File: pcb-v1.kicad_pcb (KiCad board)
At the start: 2 copper layers, 177 x 161.5 mm, 32 parts, among them J1 Conn_01x03_Socket, J10 Screw_Terminal_01x04, J11 Screw_Terminal_01x04, J12 Screw_Terminal_01x04, J13 Screw_Terminal_01x04, J14 Screw_Terminal_01x06, J15 Conn_01x06_Pin, J2 Conn_01x03_Socket, J3 Conn_01x03_Socket, J4 Conn_01x03_Socket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

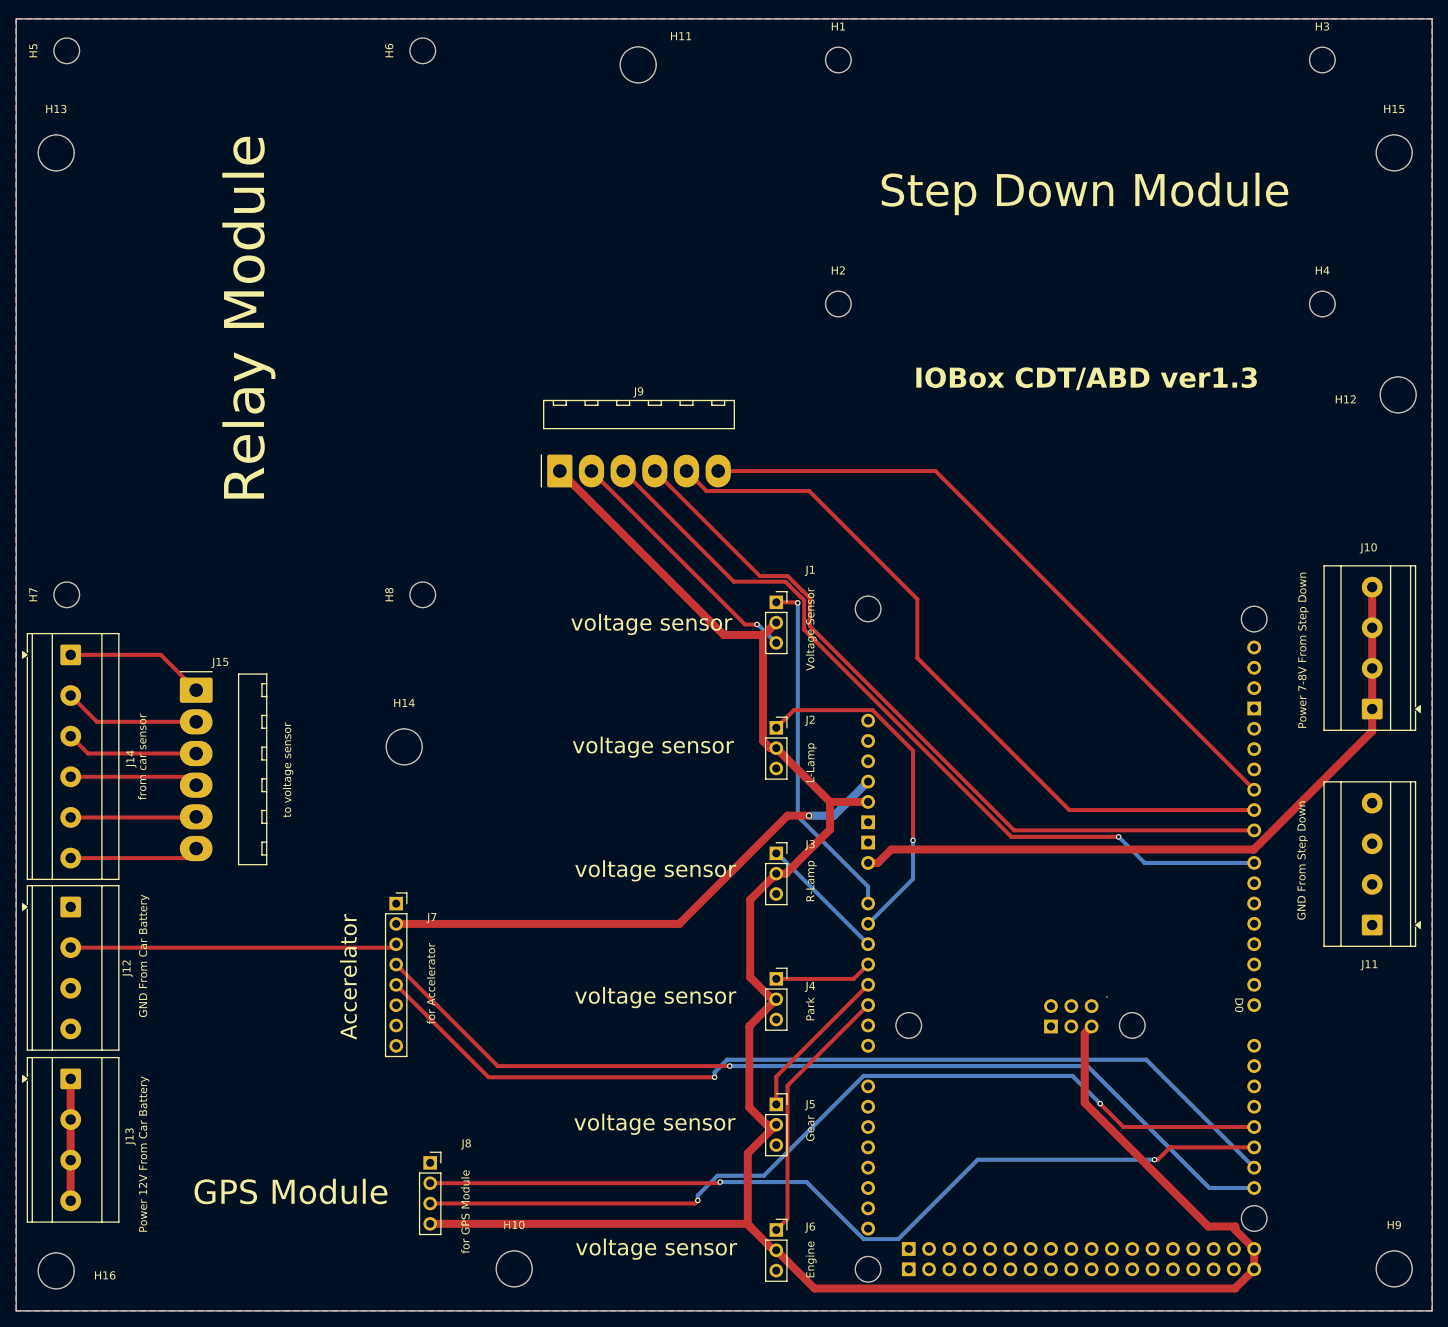
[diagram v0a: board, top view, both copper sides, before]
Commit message: adjust foot print to small size
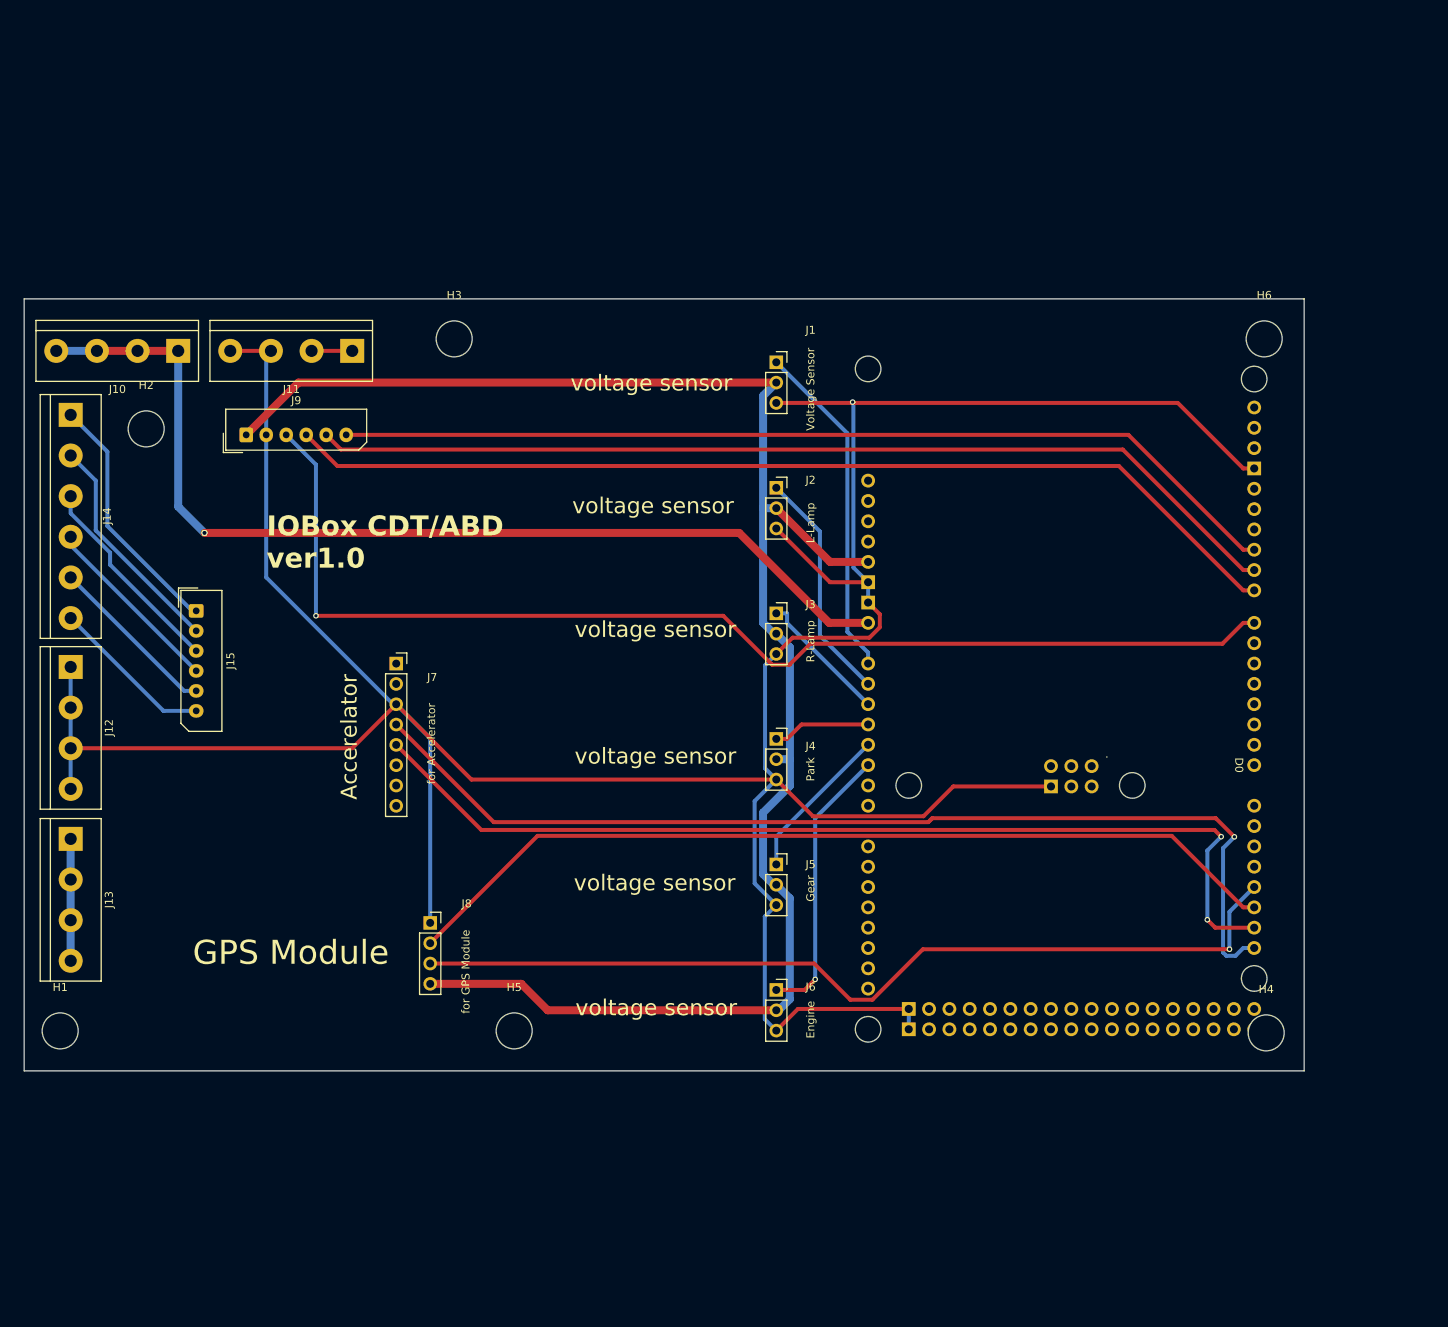
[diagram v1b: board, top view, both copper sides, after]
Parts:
- removed H10, H11, H12, H13, H14, H15, H16, H9: MountingHole, MountingHole:MountingHole_4.5mm
- removed H7, H8: MountingHole, MountingHole:MountingHole_3.2mm_M3
- H1, H2, H3, H4, H5, H6: footprint MountingHole:MountingHole_3.2mm_M3 -> MountingHole:MountingHole_4.5mm
- J10, J11, J12, J13: footprint TerminalBlock_Phoenix:TerminalBlock_Phoenix_MKDS-3-4-5.08_1x04_P5.08mm_Horizontal -> TerminalBlock-bornier:TerminalBlock_bornier-4_P5.08mm
- J14: footprint TerminalBlock_Phoenix:TerminalBlock_Phoenix_MKDS-3-6-5.08_1x06_P5.08mm_Horizontal -> TerminalBlock-bornier:TerminalBlock_bornier-6_P5.08mm
- J15, J9: footprint Connector_Molex:Molex_KK-396_A-41792-0006_1x06_P3.96mm_Horizontal -> Connector_Molex:Molex_SPOX_5267-06A_1x06_P2.50mm_Vertical
- moved J10 155.8 mm to (82.8, 58.0), turned to 180 degrees
- moved H1 155.5 mm to (68.0, 143.0)
- moved J11 146.3 mm to (104.5, 58.0), turned to 180 degrees
- moved H5 134.7 mm to (124.8, 143.0), turned to 0 degrees
- moved H3 114.0 mm to (117.2, 56.5)
- moved H6 111.2 mm to (218.5, 56.5), turned to 0 degrees
- moved H4 91.4 mm to (218.8, 143.2)
- moved H2 87.9 mm to (78.8, 67.8)
- moved J9 39.5 mm to (91.2, 68.5)
- moved J12 30.0 mm to (69.3, 97.5)
- moved J13 30.0 mm to (69.3, 119.0)
- moved J14 30.0 mm to (69.3, 66.0)
- moved J4 30.0 mm to (157.5, 106.5)
- moved A1 30.0 mm to (166.4, 46.3)
- moved J1 30.0 mm to (157.5, 59.4)
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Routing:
- net GND: track 72.9 -> 431.3 mm
- net /3.3VDC: track 66.4 -> 0.00 mm, vias 1 -> 0
- net /5VDC: track 281.5 -> 215.8 mm
- net Net-(J9-Pin_3): track 101.3 -> 146.1 mm
- net /VIN: track 87.8 -> 127.0 mm, vias 0 -> 1
- net Net-(J9-Pin_6): track 83.5 -> 119.4 mm
- net Net-(J9-Pin_4): track 95.6 -> 126.6 mm
- net Net-(J9-Pin_5): track 92.8 -> 123.0 mm
- net /L-Lamp: track 44.1 -> 29.3 mm, vias 1 -> 0
- net Net-(J14-Pin_1): track 17.5 -> 31.3 mm
- net /SCL: track 118.8 -> 130.9 mm
- net Net-(J14-Pin_2): track 17.1 -> 28.4 mm
- net Net-(J14-Pin_3): track 16.6 -> 25.8 mm
- net Net-(J14-Pin_4): track 16.1 -> 23.3 mm
- net /SDA: track 118.9 -> 125.2 mm, vias 1 -> 2
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- removed copper zone on B.Cu, net GND
- removed copper zone on F.Cu, net GND
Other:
- board size 177 x 161.5 mm -> 160 x 96.5 mm
- board text added: "IOBox CDT/ABD ver1.0"
- board text removed: "IOBox CDT/ABD ver1.3"
- board text removed: "Relay Module"
- board text removed: "Step Down Module"

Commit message: finish pcb
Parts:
- moved H3 49.0 mm to (68.2, 56.2)
- moved H2 47.2 mm to (124.5, 56.0)
- moved H4 15.9 mm to (206.0, 133.8)
- moved J10 9.50 mm to (92.2, 58.0)
- moved J11 8.75 mm to (113.2, 58.0)
- moved J9 2.75 mm to (91.2, 71.2)
- moved J14 1.00 mm to (69.3, 65.0)
- moved J12 0.50 mm to (69.3, 98.0)
- moved H1 0.37 mm to (68.3, 143.3)
- moved J15 0.26 mm to (85.3, 90.5)
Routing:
- net GND: track 431.3 -> 0.00 mm, vias 1 -> 0
- net /5VDC: track 215.8 -> 299.8 mm
- net /3.3VDC: track 0.00 -> 76.9 mm
- net /VIN: track 127.0 -> 106.1 mm, vias 1 -> 0
- net /L-Lamp: track 29.3 -> 43.5 mm
- net Net-(J9-Pin_3): track 146.1 -> 132.4 mm, vias 1 -> 0
- net /SCL: track 130.9 -> 118.8 mm
- net /Belt: track 42.4 -> 45.9 mm
- net /Engine: track 34.9 -> 32.9 mm, vias 1 -> 0
- net Net-(J14-Pin_5): track 21.6 -> 23.4 mm
- net Net-(J14-Pin_2): track 28.4 -> 29.9 mm
- net /TX1: track 113.5 -> 112.0 mm
- net Net-(J14-Pin_4): track 23.3 -> 24.7 mm
- net Net-(J14-Pin_3): track 25.8 -> 27.0 mm
- net Net-(J9-Pin_5): track 123.0 -> 124.0 mm
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- added copper zone on B.Cu, net GND
- added copper zone on F.Cu, net GND
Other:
- board text added: "12V"
- board text added: "5V"
- board text added: "8V"
- board text added: "Belt"
- board text added: "CH1"
- board text added: "CH2"
- board text added: "CH3"
- board text added: "CH4"
- board text added: "Engine"
- board text added: "GND"
- board text added: "Gear"
- board text added: "L-Lamp"
- board text added: "Park"
- board text added: "R-Lamp"
